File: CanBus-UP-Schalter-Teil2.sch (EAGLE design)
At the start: 18 parts, among them IC1 LM2937IMP-5.0, IC2 MEGA8-AI, IC3 MCP2515T-I/SO, Q1 EUROQUARTZ-MMJ, Q2 EUROQUARTZ-MMJ, Q3 BC847ASMD, Q4 BC847ASMD, U1 MCP2562-E/SN

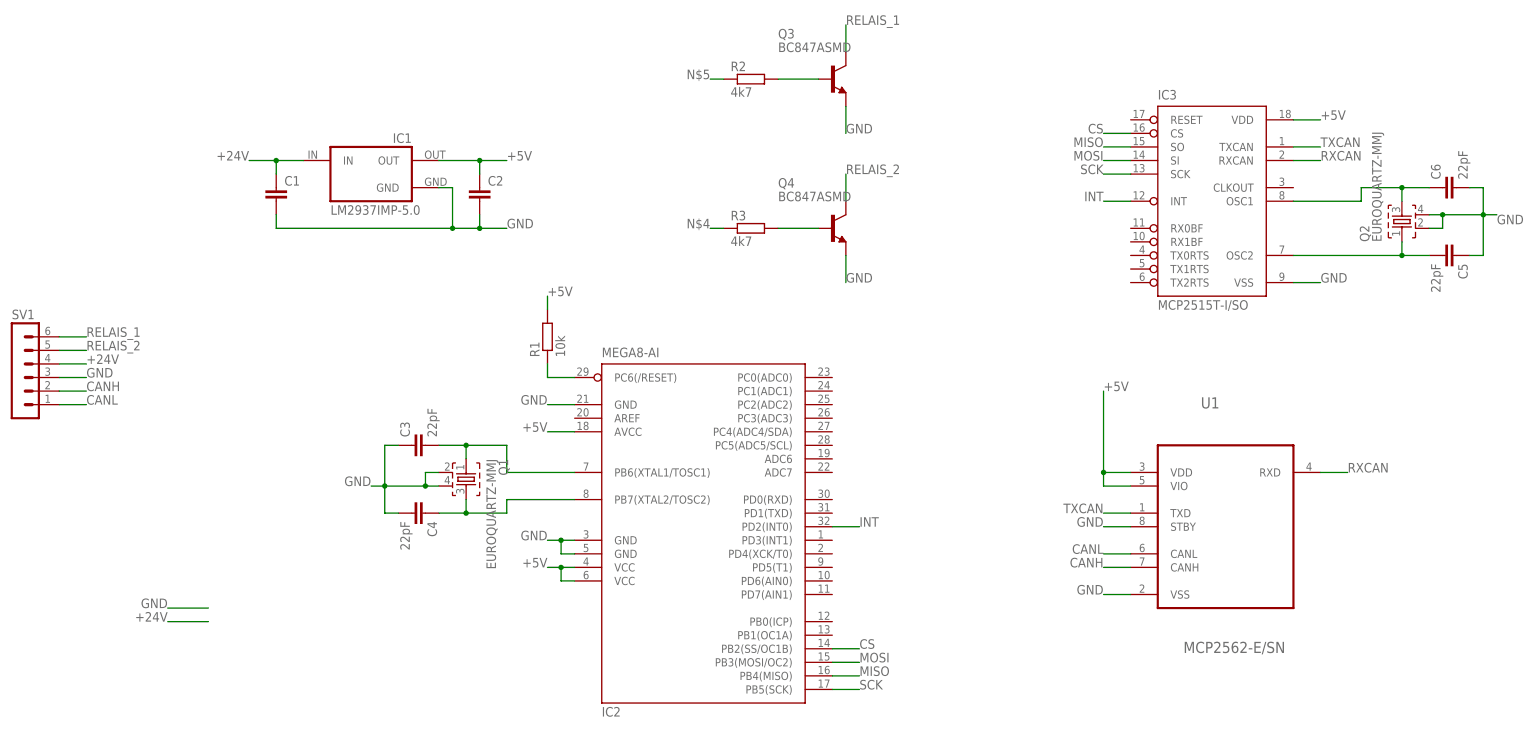
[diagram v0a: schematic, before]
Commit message: Updated CAN-Bus UP-Schalter
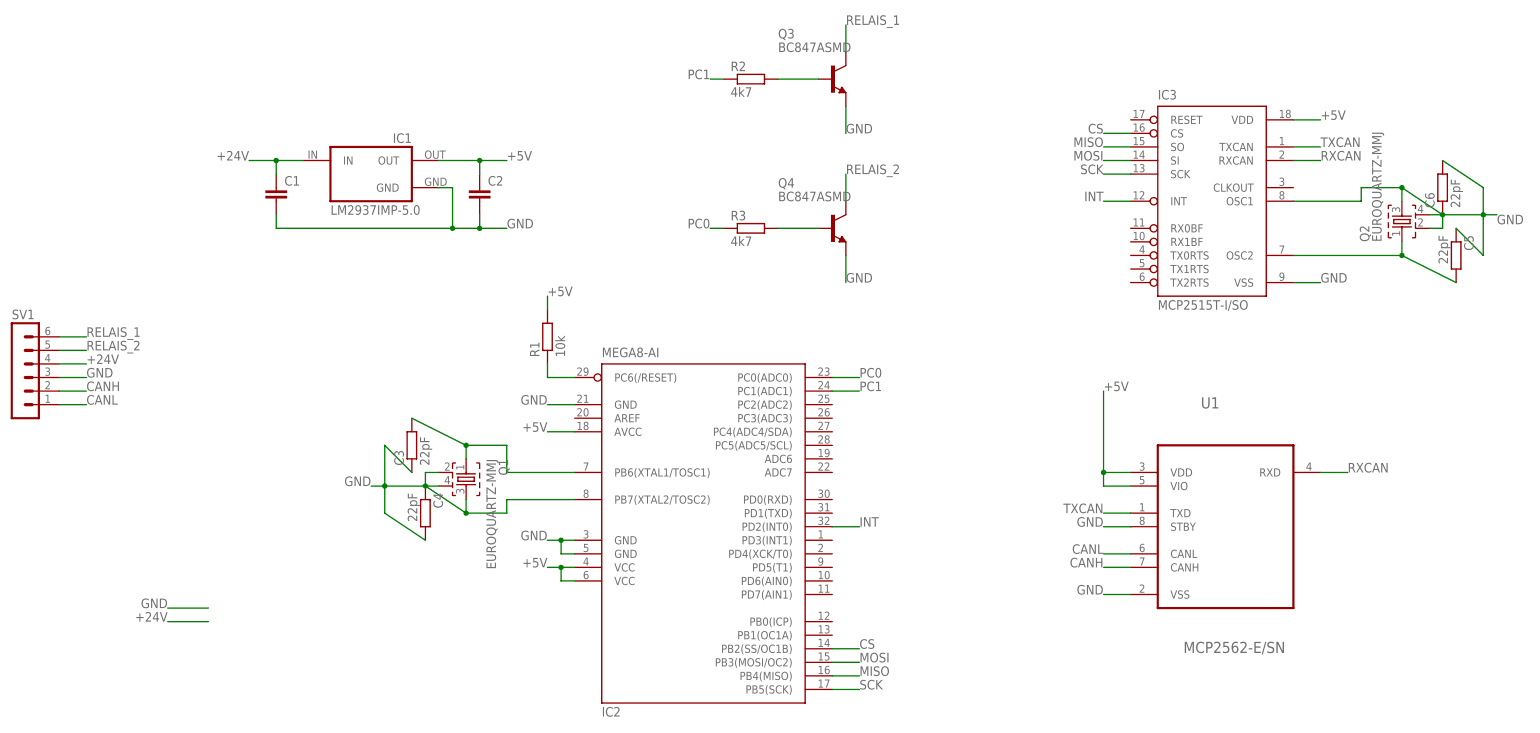
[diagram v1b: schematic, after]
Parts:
- C3, C4, C5, C6: device rcl:C-EUC1206 -> rcl:R-EU_R0805
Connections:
- removed net N$4: R3.1
- removed net N$5: R2.1
- new net PC0: IC2.PC0(ADC0), R3.1
- new net PC1: IC2.PC1(ADC1), R2.1
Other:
- moved on the sheet: C3, C4, C5, C6
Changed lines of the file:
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@@
 <part name="U1" library="mcp2515_2551_2562" deviceset="MCP2562" device="-E/SN"/>
 <part name="Q1" library="crystal-smd" deviceset="EUROQUARTZ-M*" device="MJ"/>
-<part name="C3" library="rcl" deviceset="C-EU" device="C1206" value="22pF"/>
-<part name="C4" library="rcl" deviceset="C-EU" device="C1206" value="22pF"/>
+<part name="C3" library="rcl" deviceset="R-EU_" device="R0805" value="22pF"/>
+<part name="C4" library="rcl" deviceset="R-EU_" device="R0805" value="22pF"/>
 <part name="Q2" library="crystal-smd" deviceset="EUROQUARTZ-M*" device="MJ"/>
-<part name="C5" library="rcl" deviceset="C-EU" device="C1206" value="22pF"/>
-<part name="C6" library="rcl" deviceset="C-EU" device="C1206" value="22pF"/>
+<part name="C5" library="rcl" deviceset="R-EU_" device="R0805" value="22pF"/>
+<part name="C6" library="rcl" deviceset="R-EU_" device="R0805" value="22pF"/>
 <part name="R1" library="rcl" deviceset="R-EU_" device="R1206" value="10k"/>
 <part name="Q3" library="transistor-npn" deviceset="BC847*" device="SMD" technology="A"/>
@@
 <junction x="116.84" y="91.44"/>
 <pinref part="C3" gate="G$1" pin="1"/>
-<wire x1="111.76" y1="99.06" x2="109.22" y2="99.06" width="0.1524" layer="91"/>
+<wire x1="114.3" y1="93.98" x2="109.22" y2="99.06" width="0.1524" layer="91"/>
 <pinref part="C4" gate="G$1" pin="2"/>
-<wire x1="111.76" y1="86.36" x2="109.22" y2="86.36" width="0.1524" layer="91"/>
+<wire x1="116.84" y1="81.28" x2="109.22" y2="86.36" width="0.1524" layer="91"/>
 <wire x1="109.22" y1="99.06" x2="109.22" y2="91.44" width="0.1524" layer="91"/>
 <wire x1="109.22" y1="91.44" x2="109.22" y2="86.36" width="0.1524" layer="91"/>
@@
 <junction x="307.34" y="142.24"/>
 <pinref part="C5" gate="G$1" pin="1"/>
-<wire x1="312.42" y1="134.62" x2="314.96" y2="134.62" width="0.1524" layer="91"/>
+<wire x1="309.88" y1="139.7" x2="314.96" y2="134.62" width="0.1524" layer="91"/>
 <pinref part="C6" gate="G$1" pin="2"/>
-<wire x1="312.42" y1="147.32" x2="314.96" y2="147.32" width="0.1524" layer="91"/>
+<wire x1="307.34" y1="152.4" x2="314.96" y2="147.32" width="0.1524" layer="91"/>
 <wire x1="314.96" y1="134.62" x2="314.96" y2="142.24" width="0.1524" layer="91"/>
 <wire x1="314.96" y1="142.24" x2="314.96" y2="147.32" width="0.1524" layer="91"/>
@@
 <wire x1="124.46" y1="99.06" x2="124.46" y2="96.52" width="0.1524" layer="91"/>
 <pinref part="C3" gate="G$1" pin="2"/>
-<wire x1="119.38" y1="99.06" x2="124.46" y2="99.06" width="0.1524" layer="91"/>
+<wire x1="114.3" y1="104.14" x2="124.46" y2="99.06" width="0.1524" layer="91"/>
 <junction x="124.46" y="99.06"/>
 </segment>
@@
 <wire x1="124.46" y1="86.36" x2="124.46" y2="88.9" width="0.1524" layer="91"/>
 <pinref part="C4" gate="G$1" pin="1"/>
-<wire x1="119.38" y1="86.36" x2="124.46" y2="86.36" width="0.1524" layer="91"/>
+<wire x1="116.84" y1="91.44" x2="124.46" y2="86.36" width="0.1524" layer="91"/>
 <junction x="124.46" y="86.36"/>
 </segment>
@@
 <wire x1="299.72" y1="134.62" x2="299.72" y2="137.16" width="0.1524" layer="91"/>
 <pinref part="C5" gate="G$1" pin="2"/>
-<wire x1="304.8" y1="134.62" x2="299.72" y2="134.62" width="0.1524" layer="91"/>
+<wire x1="309.88" y1="129.54" x2="299.72" y2="134.62" width="0.1524" layer="91"/>
 <junction x="299.72" y="134.62"/>
 <pinref part="IC3" gate="G$1" pin="OSC2"/>
@@
 <wire x1="299.72" y1="147.32" x2="299.72" y2="144.78" width="0.1524" layer="91"/>
 <pinref part="C6" gate="G$1" pin="1"/>
-<wire x1="304.8" y1="147.32" x2="299.72" y2="147.32" width="0.1524" layer="91"/>
+<wire x1="307.34" y1="142.24" x2="299.72" y2="147.32" width="0.1524" layer="91"/>
 <junction x="299.72" y="147.32"/>
 <pinref part="IC3" gate="G$1" pin="OSC1"/>
@@
 </segment>
 </net>
-<net name="N$4" class="0">
+<net name="PC1" class="0">
+<segment>
+<pinref part="IC2" gate="G$1" pin="PC1(ADC1)"/>
+<wire x1="193.04" y1="109.22" x2="198.12" y2="109.22" width="0.1524" layer="91"/>
+<label x="198.12" y="109.22" size="1.778" layer="95"/>
+</segment>
+<segment>
+<pinref part="R2" gate="G$1" pin="1"/>
+<wire x1="170.18" y1="167.64" x2="172.72" y2="167.64" width="0.1524" layer="91"/>
+<label x="170.18" y="167.64" size="1.778" layer="95" rot="MR0"/>
+</segment>
+</net>
+<net name="PC0" class="0">
+<segment>
+<pinref part="IC2" gate="G$1" pin="PC0(ADC0)"/>
+<wire x1="193.04" y1="111.76" x2="198.12" y2="111.76" width="0.1524" layer="91"/>
+<label x="198.12" y="111.76" size="1.778" layer="95"/>
+</segment>
 <segment>
 <pinref part="R3" gate="G$1" pin="1"/>
@@
 </segment>
 </net>
-<net name="N$5" class="0">
-<segment>
-<pinref part="R2" gate="G$1" pin="1"/>
-<wire x1="170.18" y1="167.64" x2="172.72" y2="167.64" width="0.1524" layer="91"/>
-<label x="170.18" y="167.64" size="1.778" layer="95" rot="MR0"/>
-</segment>
-</net>
